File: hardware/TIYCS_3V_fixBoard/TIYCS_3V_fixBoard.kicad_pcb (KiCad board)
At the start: 2 copper layers, 8 parts, among them J1 12V, J2 i2c, U1 XL-1509-3.3E1

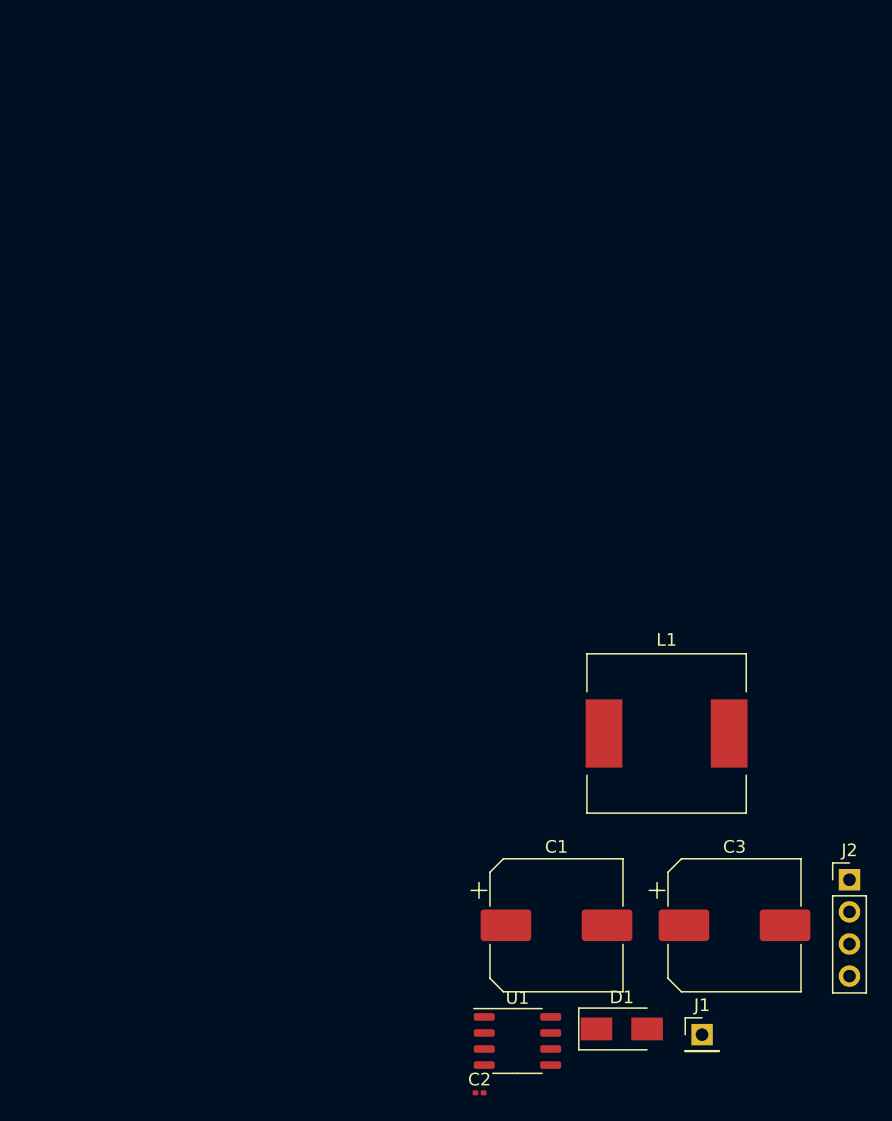
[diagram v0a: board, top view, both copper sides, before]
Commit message: Added XL-1509-3.3 on main board
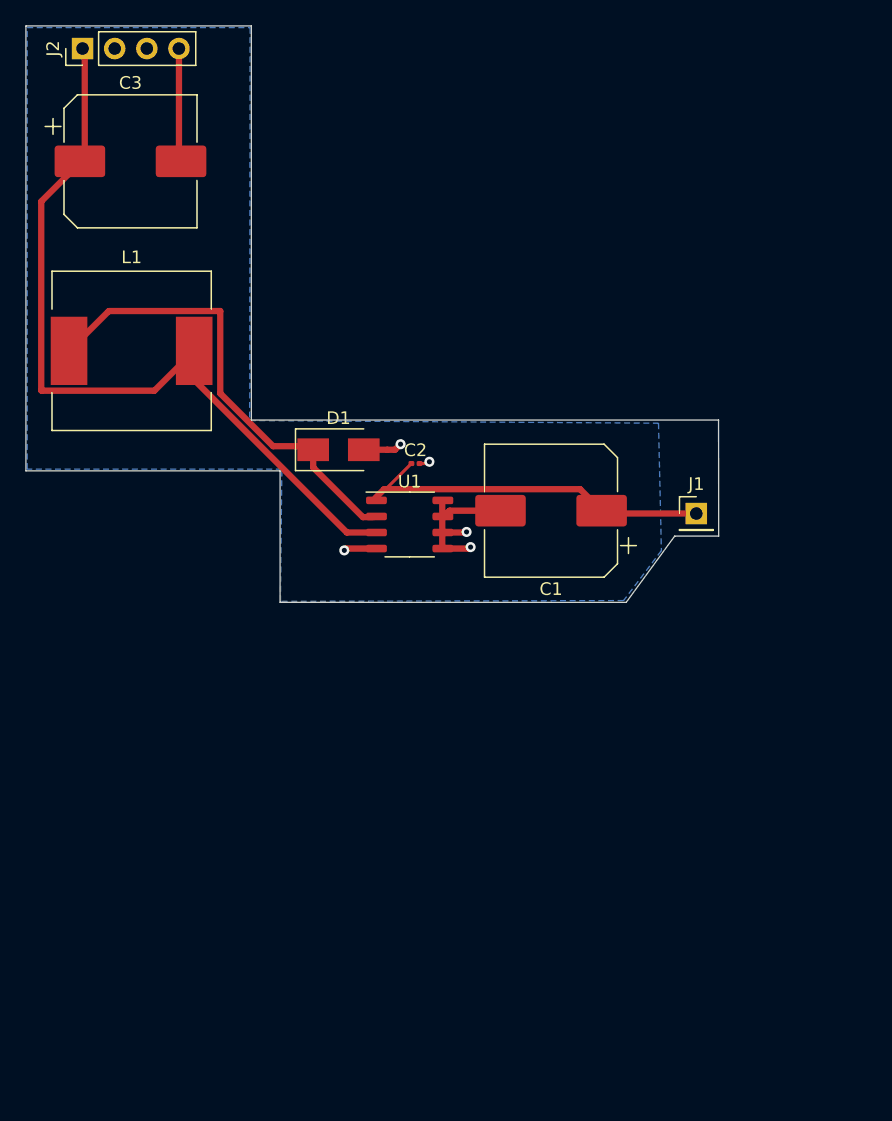
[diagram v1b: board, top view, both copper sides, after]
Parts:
- moved J2 89.4 mm to (47.5, 1.79), turned to 90 degrees
- moved C3 77.0 mm to (51.2, 10.7)
- moved L1 52.0 mm to (51.3, 25.7)
- moved D1 51.0 mm to (67.7, 33.5)
- moved C2 50.0 mm to (73.8, 34.6)
- moved U1 41.7 mm to (73.3, 39.4)
- moved J1 41.2 mm to (96.0, 38.6)
- moved C1 32.8 mm to (84.5, 38.3), turned to 180 degrees
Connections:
- net Net-(C1-Pad2) renamed GND
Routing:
- net Net-(C3-Pad1): track 0.00 -> 65.7 mm
- net Net-(D1-Pad1): track 0.00 -> 36.7 mm
- net Net-(C1-Pad1): track 0.00 -> 29.1 mm
- net GND: track 0.00 -> 28.2 mm, vias 0 -> 5
- added copper zone on B.Cu, net GND
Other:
- board outline added: 54.8 x 45.6 mm
